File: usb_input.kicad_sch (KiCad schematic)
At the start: 36 parts, among them J1 Conn_01x02_Male, J2 USB_C_Receptacle_USB2.0, Q1 DMP3036SSD, Q2 NMOS, Q5 DMP3036SSD, U2 CYPD3177

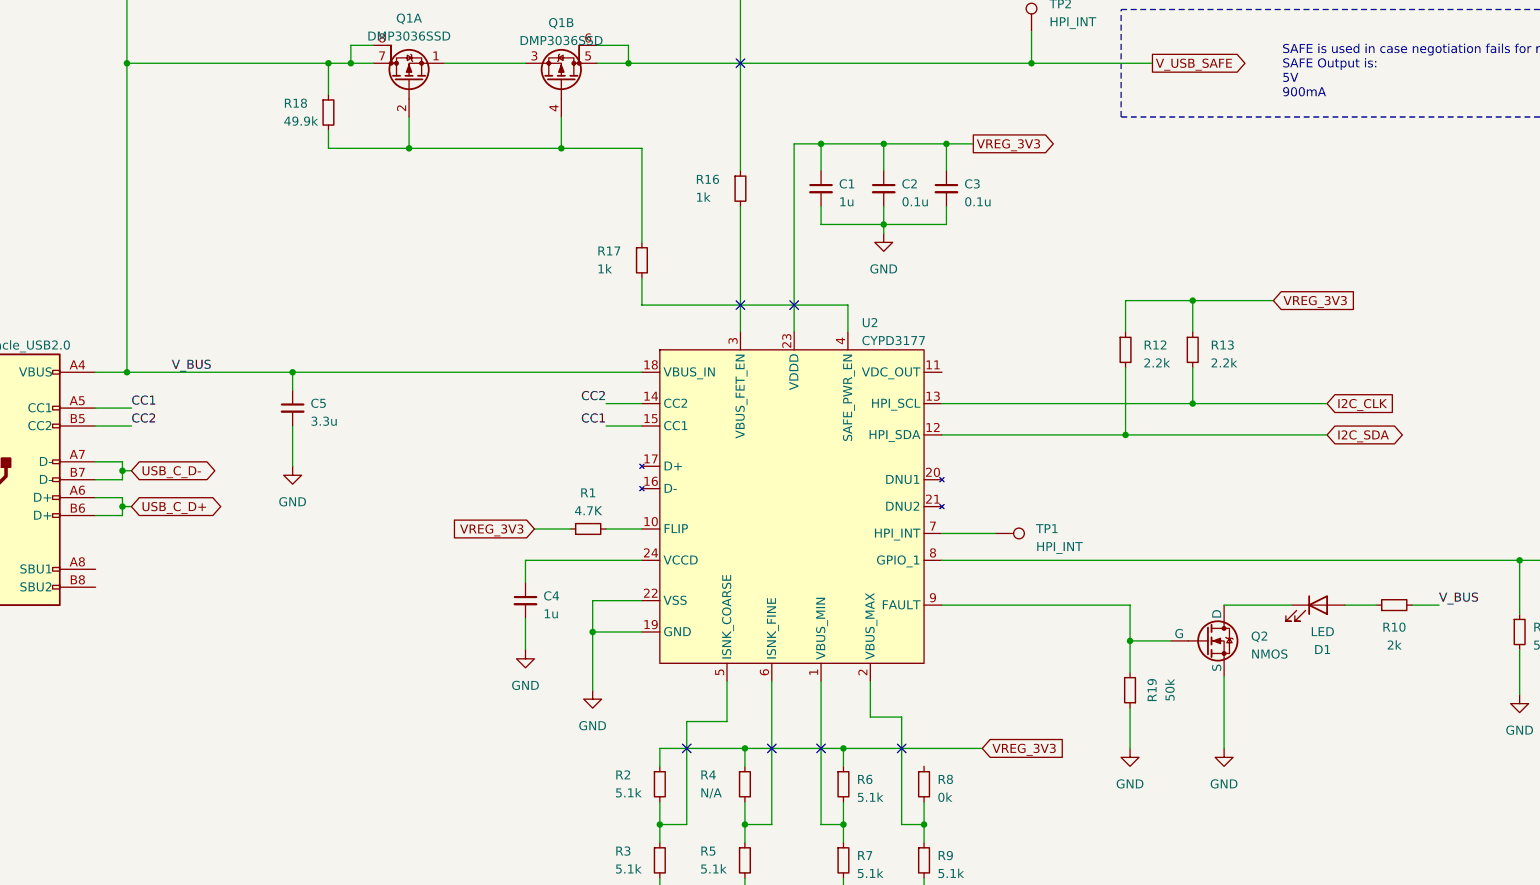
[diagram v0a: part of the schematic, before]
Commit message: Added microcontroller stage. Need to fix the supply routing to power from battery.
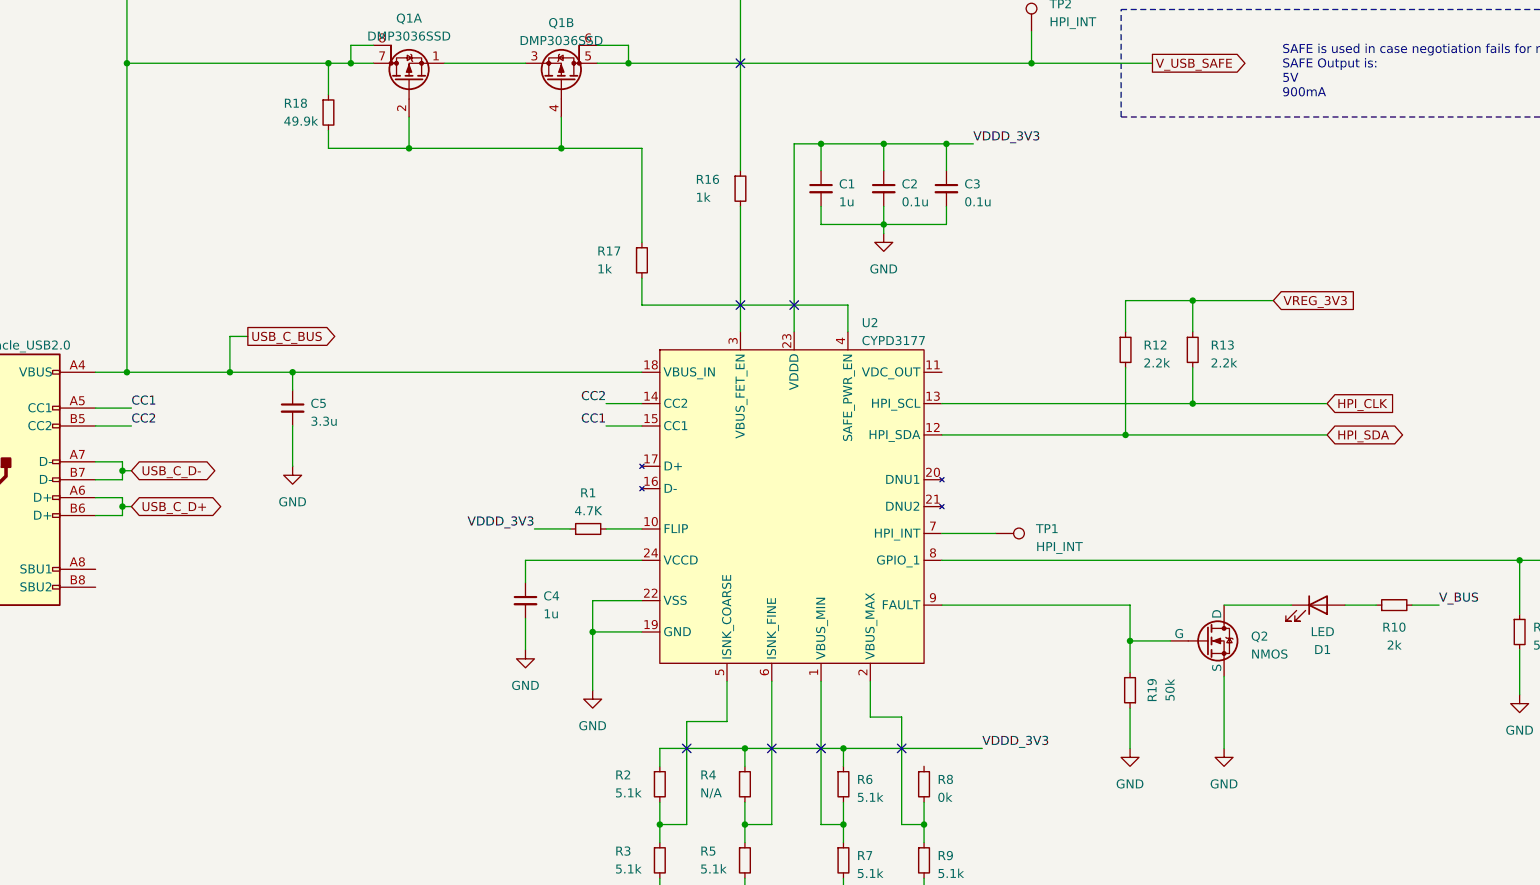
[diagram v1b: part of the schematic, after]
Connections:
- net VREG_3V3: no longer C1.1, C2.1, C3.1, R1.1, R2.1, R4.1, R6.1, U2.23 (VDDD)
- net V_BUS: no longer C5.1, C6.1, J2.A4 (VBUS), J2.A9 (VBUS), J2.B4 (VBUS), J2.B9 (VBUS), Q1.7 (D), Q1.8 (G), Q5.7 (D), Q5.8 (G), R15.1, R18.1, U2.18 (VBUS_IN)
- net I2C_CLK renamed HPI_CLK
- net I2C_SDA renamed HPI_SDA
- new net USB_C_BUS: C5.1, C6.1, J2.A4 (VBUS), J2.A9 (VBUS), J2.B4 (VBUS), J2.B9 (VBUS), Q1.7 (D), Q1.8 (G), Q5.7 (D), Q5.8 (G), R15.1, R18.1, U2.18 (VBUS_IN)
- new net VDDD_3V3: C1.1, C2.1, C3.1, R1.1, R2.1, R4.1, R6.1, U2.23 (VDDD)
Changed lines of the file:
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@@
   (junction (at 214.63 63.5) (diameter 0) (color 0 0 0 0)
+  )
+  (junction (at 148.59 121.92) (diameter 0) (color 0 0 0 0)
   )
   (junction (at 180.34 45.085) (diameter 0) (color 0 0 0 0)
@@
     (stroke (width 0) (type default))
   )
+  (wire (pts (xy 148.59 116.84) (xy 148.59 121.92))
+    (stroke (width 0) (type default))
+  )
   (wire (pts (xy 285.115 111.76) (xy 285.115 116.205))
     (stroke (width 0) (type default))
@@
     (stroke (width 0) (type default))
   )
-  (wire (pts (xy 133.985 121.92) (xy 157.48 121.92))
+  (wire (pts (xy 133.985 121.92) (xy 148.59 121.92))
     (stroke (width 0) (type default))
   )
@@
     (stroke (width 0) (type default))
   )
+  (wire (pts (xy 148.59 121.92) (xy 157.48 121.92))
+    (stroke (width 0) (type default))
+  )
   (wire (pts (xy 232.41 186.055) (xy 235.585 186.055))
     (stroke (width 0) (type default))
@@
   )
   (wire (pts (xy 173.99 90.17) (xy 162.56 90.17))
+    (stroke (width 0) (type default))
+  )
+  (wire (pts (xy 151.13 116.84) (xy 148.59 116.84))
     (stroke (width 0) (type default))
   )
@@
     (effects (font (size 1.27 1.27)) (justify left bottom))
   )
-  (label "V_BUS" (at 140.335 121.92 0) (fields_autoplaced)
-    (effects (font (size 1.27 1.27)) (justify left bottom))
-  )
   (label "CC2" (at 201.93 126.365 180) (fields_autoplaced)
     (effects (font (size 1.27 1.27)) (justify right bottom))
@@
     (effects (font (size 1.27 1.27)) (justify left bottom))
   )
+  (label "VDDD_3V3" (at 254 89.535 0) (fields_autoplaced)
+    (effects (font (size 1.27 1.27)) (justify left bottom))
+  )
   (label "CC2" (at 134.62 129.54 0) (fields_autoplaced)
     (effects (font (size 1.27 1.27)) (justify left bottom))
   )
+  (label "VDDD_3V3" (at 191.77 144.145 180) (fields_autoplaced)
+    (effects (font (size 1.27 1.27)) (justify right bottom))
+  )
   (label "V_BUS" (at 320.04 154.94 0) (fields_autoplaced)
     (effects (font (size 1.27 1.27)) (justify left bottom))
   )
-  (global_label "VREG_3V3" (shape output) (at 254 89.535 0) (fields_autoplaced)
-    (effects (font (size 1.27 1.27)) (justify left))
-    (property "Intersheetrefs" "${INTERSHEET_REFS}" (at 266.1586 89.535 0)
-      (effects (font (size 1.27 1.27)) (justify left) hide)
-    )
-  )
-  (global_label "I2C_SDA" (shape bidirectional) (at 304.165 130.81 0) (fields_autoplaced)
-    (effects (font (size 1.27 1.27)) (justify left))
-    (property "Intersheetrefs" "${INTERSHEET_REFS}" (at 315.8021 130.81 0)
-      (effects (font (size 1.27 1.27)) (justify left) hide)
-    )
-  )
-  (global_label "VREG_3V3" (shape input) (at 255.27 175.26 0) (fields_autoplaced)
-    (effects (font (size 1.27 1.27)) (justify left))
-    (property "Intersheetrefs" "${INTERSHEET_REFS}" (at 267.4286 175.26 0)
+  (label "VDDD_3V3" (at 255.27 175.26 0) (fields_autoplaced)
+    (effects (font (size 1.27 1.27)) (justify left bottom))
+  )
+  (global_label "HPI_SDA" (shape bidirectional) (at 304.165 130.81 0) (fields_autoplaced)
+    (effects (font (size 1.27 1.27)) (justify left))
+    (property "Intersheetrefs" "${INTERSHEET_REFS}" (at 315.9231 130.81 0)
       (effects (font (size 1.27 1.27)) (justify left) hide)
     )
@@
     )
   )
-  (global_label "I2C_CLK" (shape input) (at 304.165 126.365 0) (fields_autoplaced)
-    (effects (font (size 1.27 1.27)) (justify left))
-    (property "Intersheetrefs" "${INTERSHEET_REFS}" (at 314.6908 126.365 0)
+  (global_label "HPI_CLK" (shape input) (at 304.165 126.365 0) (fields_autoplaced)
+    (effects (font (size 1.27 1.27)) (justify left))
+    (property "Intersheetrefs" "${INTERSHEET_REFS}" (at 314.8118 126.365 0)
       (effects (font (size 1.27 1.27)) (justify left) hide)
     )
@@
     )
   )
+  (global_label "USB_C_BUS" (shape output) (at 151.13 116.84 0) (fields_autoplaced)
+    (effects (font (size 1.27 1.27)) (justify left))
+    (property "Intersheetrefs" "${INTERSHEET_REFS}" (at 164.861 116.84 0)
+      (effects (font (size 1.27 1.27)) (justify left) hide)
+    )
+  )
   (global_label "VREG_3V3" (shape input) (at 296.545 111.76 0) (fields_autoplaced)
     (effects (font (size 1.27 1.27)) (justify left))
@@
     )
   )
-  (global_label "VREG_3V3" (shape input) (at 191.77 144.145 180) (fields_autoplaced)
-    (effects (font (size 1.27 1.27)) (justify right))
-    (property "Intersheetrefs" "${INTERSHEET_REFS}" (at 179.6114 144.145 0)
-      (effects (font (size 1.27 1.27)) (justify right) hide)
-    )
-  )

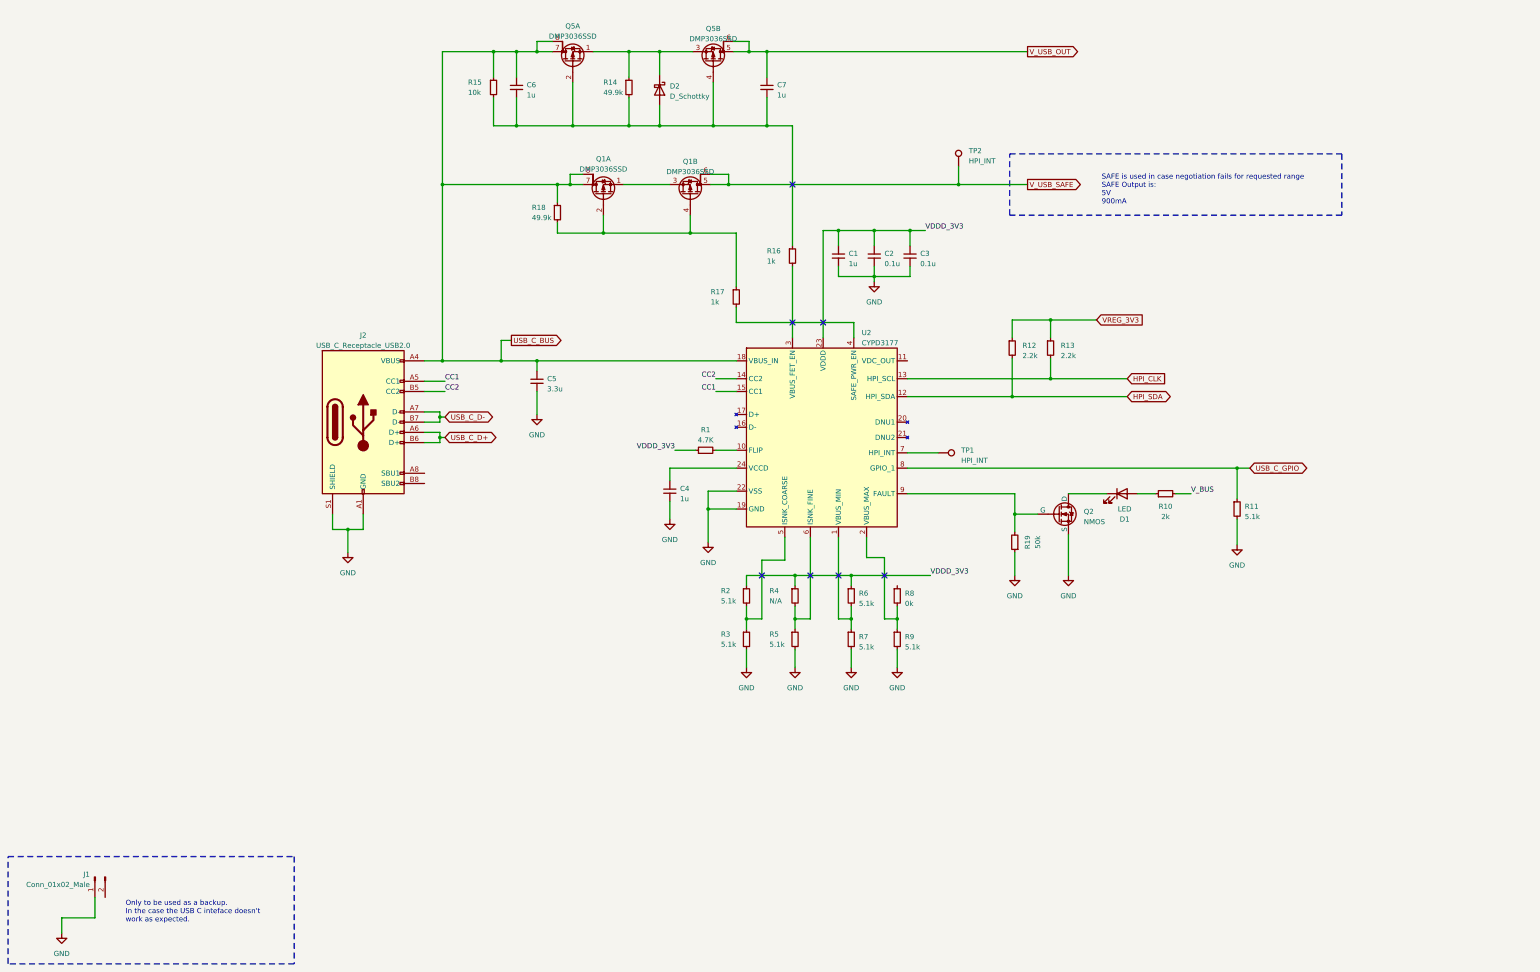
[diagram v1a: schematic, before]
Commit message: Schematic completed. Started routing.
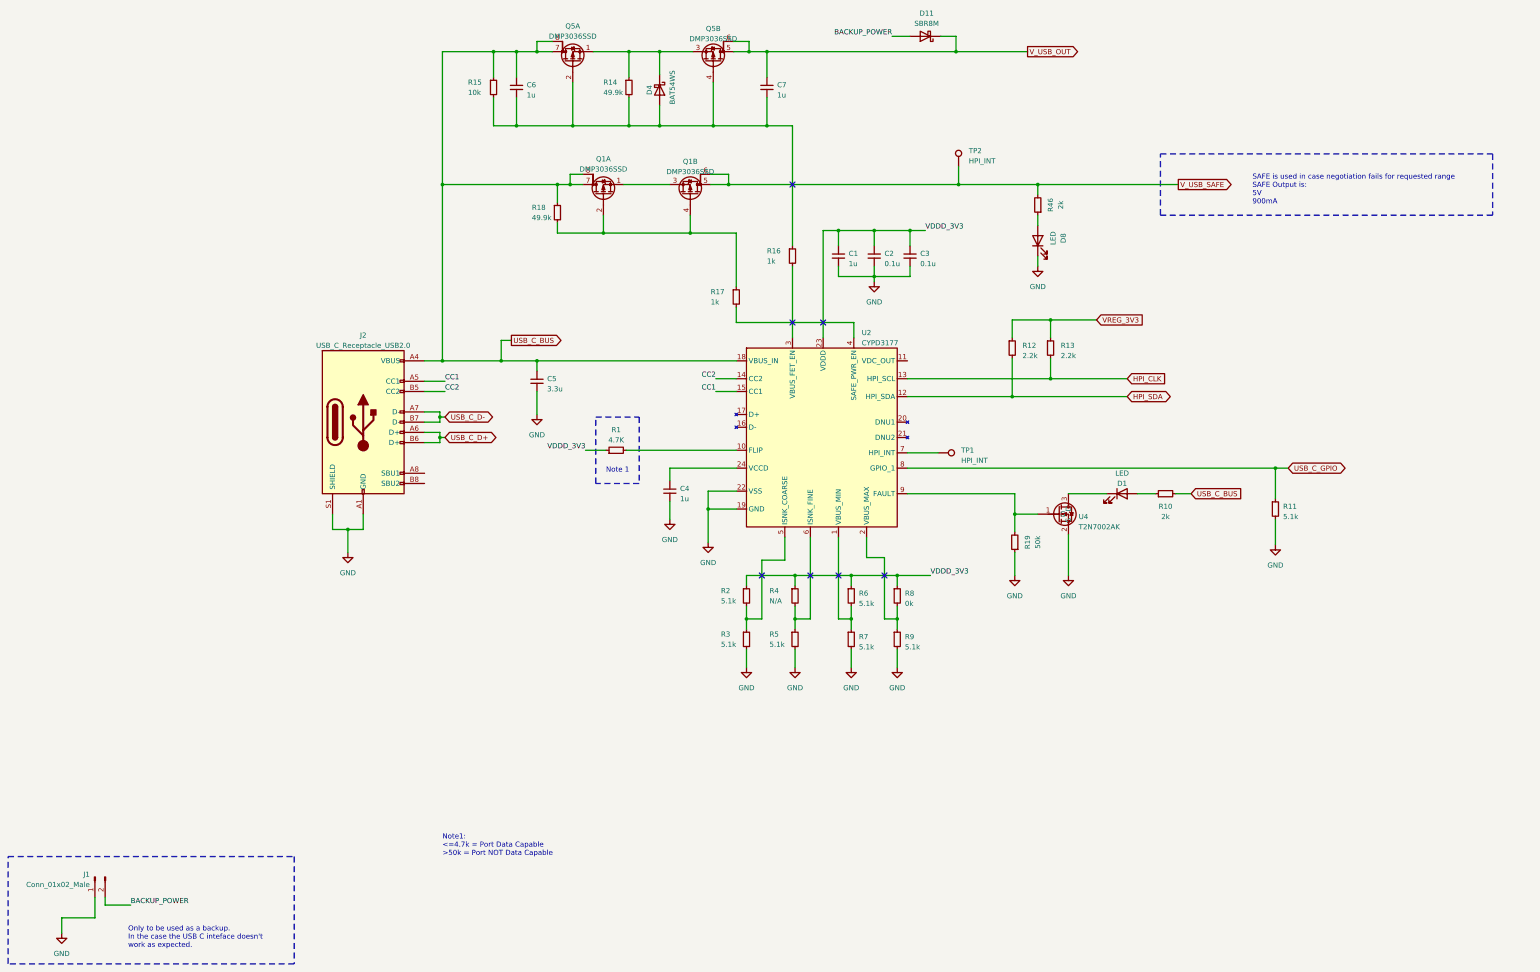
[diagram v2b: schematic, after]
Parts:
- removed D2: D_Schottky, symbol Device:D_Schottky
- removed Q2: NMOS, symbol Simulation_SPICE:NMOS
- added D11: SBR8M, Diode_SMD:D_PowerDI-5, symbol Device:D_Schottky
- added D4: BAT54WS, Diode_SMD:D_SOD-323_HandSoldering, symbol Device:D_Schottky
- added D8: LED, LED_SMD:LED_0805_2012Metric_Pad1.15x1.40mm_HandSolder, symbol Device:LED
- added R46: 2k, Resistor_SMD:R_0805_2012Metric_Pad1.20x1.40mm_HandSolder, symbol Device:R_Small
- added U4: T2N7002AK, Package_TO_SOT_SMD:SOT-23, symbol User_MOSFET:T2N7002AK,LM
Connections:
- net V_BUS is gone; now on net USB_C_BUS: R10.2
- net GND: now also D8.1 (K), U4.2 (S)
- net VDDD_3V3: now also R8.1
- net V_USB_OUT: now also D11.1 (K)
- net V_USB_SAFE: now also R46.2
- net at R19.2, U2.9 (FAULT): now also U4.1 (G)
- net at D1.1 (K): now also U4.3 (D)
- net at C6.2, C7.2, Q5.2 (G)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: now also D4.2 (A)
- net at Q5.1 (S), Q5.3 (S), R14.1: now also D4.1 (K)
- net BACKUP_POWER: now reaches J1.2 (Pin_2)
- net BACKUP_POWER: now also D11.2 (A)
- new net: D8.2 (A), R46.1
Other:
- note added: "Note 1"
- note added: "Note1: <=4.7k = Port Data Capable >50k = Port NOT Data Capable"
- moved on the sheet: R1, R11

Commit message: Re-reouting the USB C CCX lines
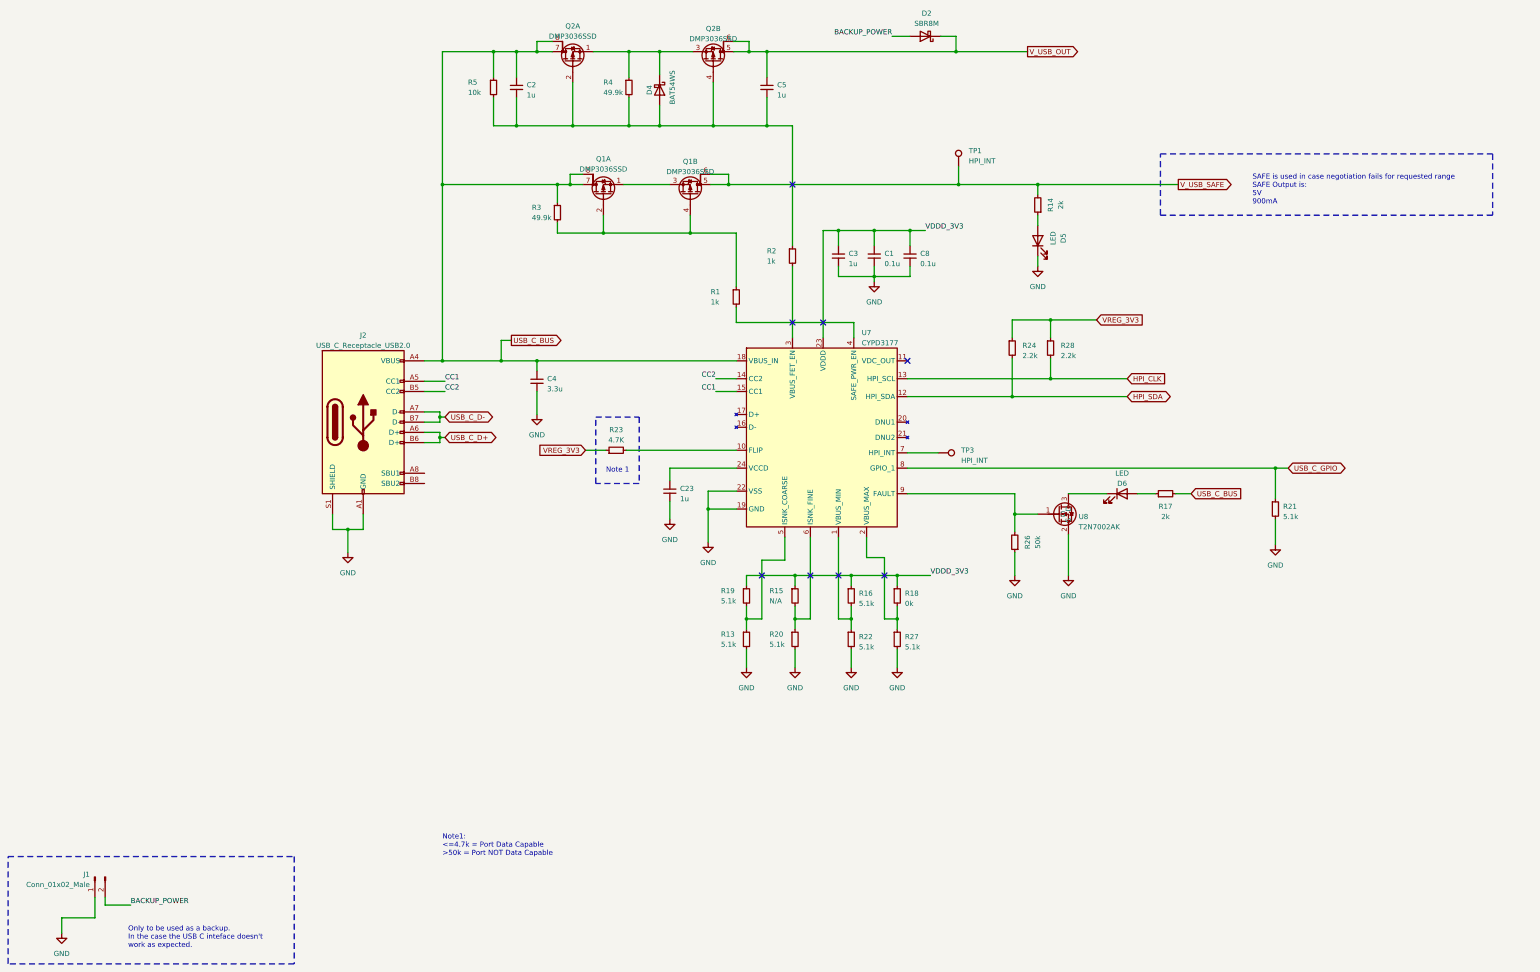
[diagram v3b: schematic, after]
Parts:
- renumbered C2 to C1, C6 to C2, C4 to C23, C1 to C3, C5 to C4, C7 to C5, C3 to C8, D11 to D2, D8 to D5, D1 to D6, Q5 to Q2, R17 to R1, R3 to R13, R46 to R14, R4 to R15, R6 to R16, R10 to R17, R8 to R18, R2 to R19, R16 to R2, R5 to R20, R11 to R21, R7 to R22, R1 to R23, R12 to R24, R19 to R26, R9 to R27, R13 to R28, R18 to R3, R14 to R4, R15 to R5, TP2 to TP1, TP1 to TP3, U2 to U7, U4 to U8
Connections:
- net VDDD_3V3: no longer R23.1
- net VREG_3V3: now also R23.1
- no-connect marks 7 -> 8
